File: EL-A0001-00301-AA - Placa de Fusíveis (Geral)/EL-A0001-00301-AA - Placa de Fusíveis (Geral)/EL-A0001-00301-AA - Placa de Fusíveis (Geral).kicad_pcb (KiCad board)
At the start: 2 copper layers, 159 x 109 mm, 25 parts, among them J1 1-776087-1, J10 AUX_POWER, J4 DC_CONVERTER, J5 VBAT, J6 UNFUSED, J7 CS_POWER, J9 ISOL_POWER

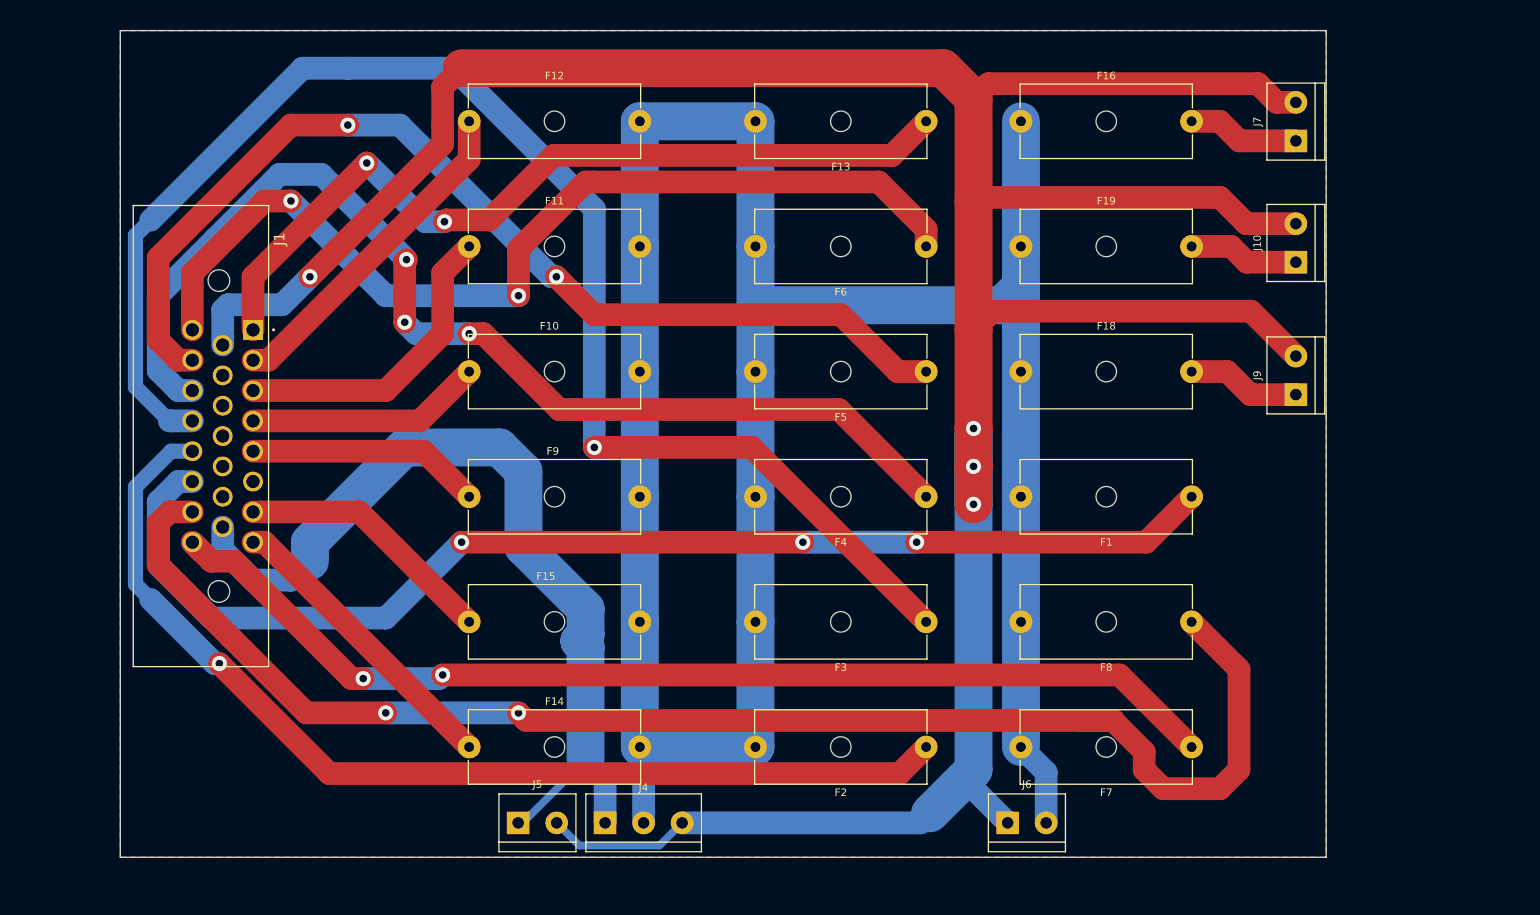
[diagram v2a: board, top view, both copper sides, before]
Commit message: FIX: panel border
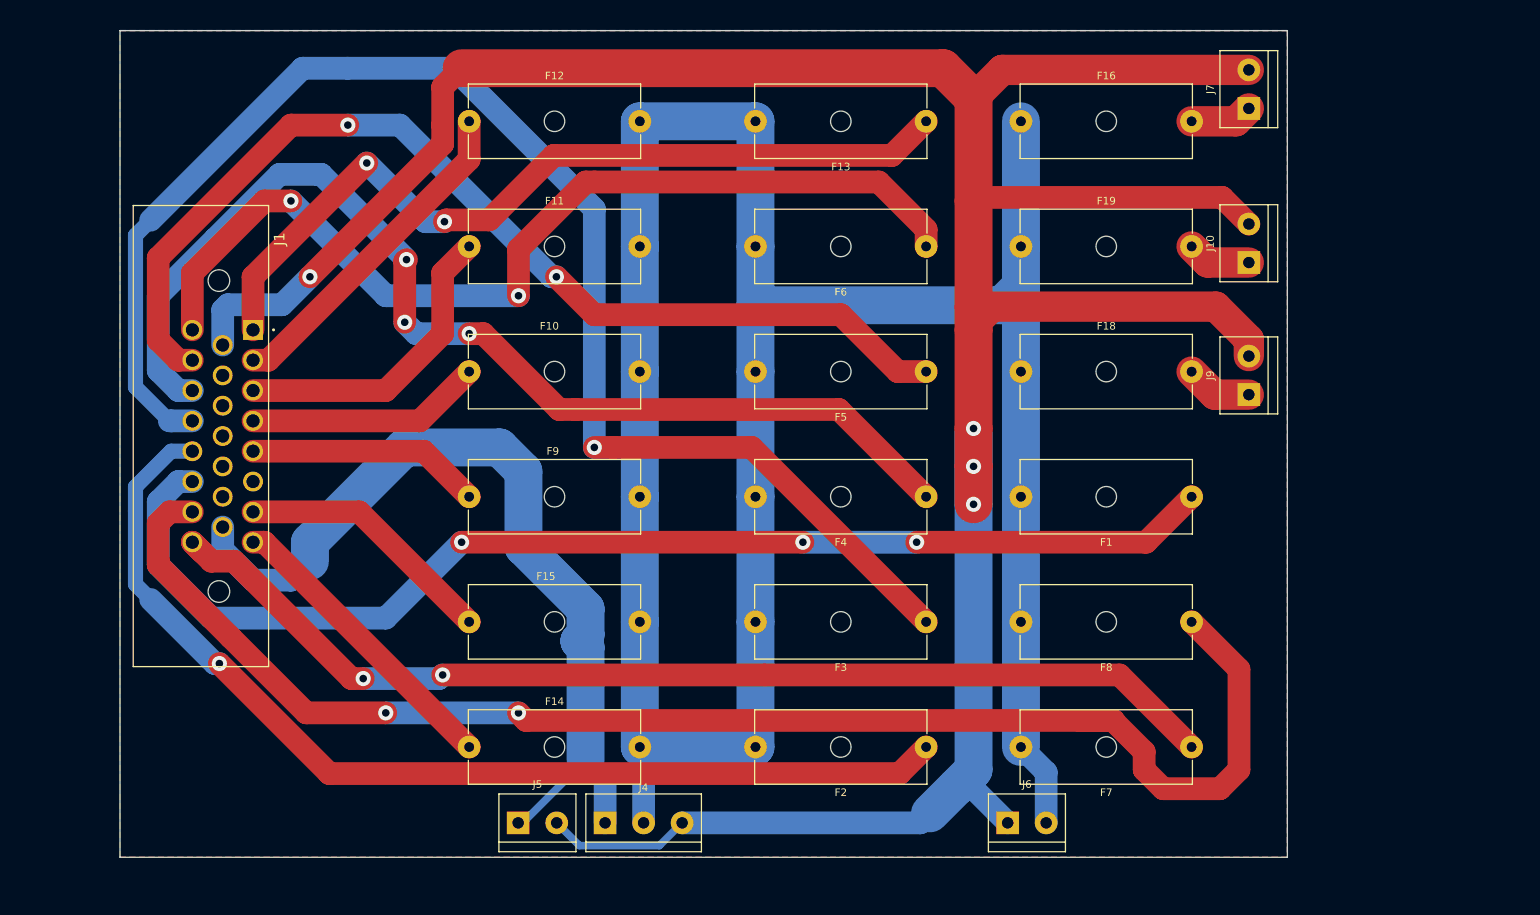
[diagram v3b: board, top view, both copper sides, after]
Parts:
- moved J7 7.53 mm to (177.8, 48.3)
- moved J10 6.20 mm to (177.8, 68.6)
- moved J9 6.20 mm to (177.8, 86.0)
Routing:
- net GNDREF: track 424.9 -> 412.8 mm
- net Net-(J7-Pad1): track 14.8 -> 8.25 mm
- net Net-(F18-Pad2): track 15.0 -> 8.81 mm
- net Net-(F19-Pad2): track 14.6 -> 8.43 mm
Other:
- board size 159 x 109 mm -> 153.9 x 109 mm
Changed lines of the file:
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@@
     (pad "2" thru_hole circle (at 22.5 0) (size 3 3) (drill 1.3) (layers *.Cu *.Mask)
       (net 2 "12V") (pintype "passive"))
-    (model "${KICAD6_3DMODEL_DIR}/Fuse.3dshapes/Fuseholder_Cylinder-5x20mm_Schurter_0031_8201_Horizontal_Open.wrl"
+    (model "${KICAD6_3DMODEL_DIR}/Fuse.3dshapes/Fuseholder_Cylinder-5x20mm_Schurter_0031_8201_Horizontal_Open.step"
       (offset (xyz 0 0 0))
       (scale (xyz 1 1 1))
@@
   )
   (footprint "TerminalBlock:TerminalBlock_bornier-2_P5.08mm" (layer "F.Cu")
-    (at 184 68.54 90)
+    (at 177.8 68.58 90)
     (descr "simple 2-pin terminal block, pitch 5.08mm, revamped version of bornier2")
     (tags "terminal block bornier2")
@@
   )
   (footprint "TerminalBlock:TerminalBlock_bornier-2_P5.08mm" (layer "F.Cu")
-    (at 184 52.54 90)
+    (at 177.8 48.26 90)
     (descr "simple 2-pin terminal block, pitch 5.08mm, revamped version of bornier2")
     (tags "terminal block bornier2")
@@
     (pad "23" thru_hole circle locked (at 28 8 270) (size 2.625 2.625) (drill 1.75) (layers *.Cu *.Mask)
       (net 16 "Net-(J1-Pad23)") (pinfunction "23") (pintype "passive"))
+    (model "C:/Users/Cheetah E-Racing/Documents/tele/Placas/Componentes/Ampseal 23/1-776087-1.step"
+      (offset (xyz 14 -36 12.5))
+      (scale (xyz 1 1 1))
+      (rotate (xyz -90 0 0))
+    )
   )
   (footprint "Fuse:Fuseholder_Cylinder-5x20mm_Schurter_0031_8201_Horizontal_Open" (layer "F.Cu")
@@
     (pad "2" thru_hole circle (at 5.08 0) (size 3 3) (drill 1.52) (layers *.Cu *.Mask)
       (net 2 "12V") (pinfunction "Pin_2") (pintype "passive"))
-    (model "${KICAD6_3DMODEL_DIR}/TerminalBlock.3dshapes/TerminalBlock_bornier-2_P5.08mm.wrl"
-      (offset (xyz 2.539999962 0 0))
+    (model "${KICAD6_3DMODEL_DIR}/TerminalBlock_Phoenix.3dshapes/TerminalBlock_Phoenix_MKDS-3-2-5.08_1x02_P5.08mm_Horizontal.step"
+      (offset (xyz 0 0 0))
       (scale (xyz 1 1 1))
       (rotate (xyz 0 0 0))
@@
   )
   (footprint "TerminalBlock:TerminalBlock_bornier-2_P5.08mm" (layer "F.Cu")
-    (at 184 86 90)
+    (at 177.8 86 90)
     (descr "simple 2-pin terminal block, pitch 5.08mm, revamped version of bornier2")
     (tags "terminal block bornier2")
@@
     (pad "2" thru_hole circle (at 22.5 0) (size 3 3) (drill 1.3) (layers *.Cu *.Mask)
       (net 2 "12V") (pintype "passive"))
-    (model "${KICAD6_3DMODEL_DIR}/Fuse.3dshapes/Fuseholder_Cylinder-5x20mm_Schurter_0031_8201_Horizontal_Open.wrl"
+    (model "${KICAD6_3DMODEL_DIR}/Fuse.3dshapes/Fuseholder_Cylinder-5x20mm_Schurter_0031_8201_Horizontal_Open.step"
       (offset (xyz 0 0 0))
       (scale (xyz 1 1 1))
@@
     )
   )
-  (gr_rect (start 29 38) (end 188 147) (layer "Edge.Cuts") (width 0.1) (fill none))
+  (gr_rect (start 28.96 38) (end 182.88 147) (layer "Edge.Cuts") (width 0.1) (fill none))
   (segment (start 164.25 105.46) (end 134 105.46) (width 3) (layer "F.Cu") (net 1))
   (segment (start 119 105.46) (end 74 105.46) (width 3) (layer "F.Cu") (net 1))
@@
   (segment (start 48 105.46) (end 46.5 105.46) (width 3) (layer "F.Cu") (net 10))
   (segment (start 75 132.46) (end 48 105.46) (width 3) (layer "F.Cu") (net 10))
-  (segment (start 170.25 82.96) (end 174.96 82.96) (width 3) (layer "F.Cu") (net 11))
-  (segment (start 174.96 82.96) (end 178 86) (width 3) (layer "F.Cu") (net 11))
-  (segment (start 178 86) (end 184 86) (width 3) (layer "F.Cu") (net 11))
-  (segment (start 177.54 68.54) (end 175.46 66.46) (width 3) (layer "F.Cu") (net 12))
-  (segment (start 184 68.54) (end 177.54 68.54) (width 3) (layer "F.Cu") (net 12))
-  (segment (start 175.46 66.46) (end 170.25 66.46) (width 3) (layer "F.Cu") (net 12))
+  (segment (start 170.25 82.96) (end 173.29 86) (width 4) (layer "F.Cu") (net 11))
+  (segment (start 173.29 86) (end 177.8 86) (width 4) (layer "F.Cu") (net 11))
+  (segment (start 172.37 68.58) (end 177.8 68.58) (width 4) (layer "F.Cu") (net 12))
+  (segment (start 170.25 66.46) (end 172.37 68.58) (width 4) (layer "F.Cu") (net 12))
   (segment (start 64 85.46) (end 46.5 85.46) (width 3) (layer "F.Cu") (net 13))
   (segment (start 75 66.46) (end 71.5 69.96) (width 3) (layer "F.Cu") (net 13))
@@
   (segment (start 46.5 101.46) (end 60.5 101.46) (width 3) (layer "F.Cu") (net 19))
   (segment (start 60.5 101.46) (end 75 115.96) (width 3) (layer "F.Cu") (net 19))
-  (segment (start 173.96 49.96) (end 176.54 52.54) (width 3) (layer "F.Cu") (net 20))
-  (segment (start 176.54 52.54) (end 184 52.54) (width 3) (layer "F.Cu") (net 20))
-  (segment (start 170.25 49.96) (end 173.96 49.96) (width 3) (layer "F.Cu") (net 20))
+  (segment (start 170.25 49.96) (end 176.1 49.96) (width 4) (layer "F.Cu") (net 20))
+  (segment (start 176.1 49.96) (end 177.8 48.26) (width 4) (layer "F.Cu") (net 20))
   (segment (start 71.5 45.46) (end 74 42.96) (width 3) (layer "F.Cu") (net 21))
   (segment (start 143.46 45) (end 141.5 46.96) (width 3) (layer "F.Cu") (net 21))
+  (segment (start 174.3 60) (end 177.8 63.5) (width 3) (layer "F.Cu") (net 21))
+  (segment (start 177.8 80.92) (end 177.8 78.74) (width 4) (layer "F.Cu") (net 21))
   (segment (start 74 42.96) (end 137.5 42.96) (width 5) (layer "F.Cu") (net 21))
-  (segment (start 179 45) (end 143.46 45) (width 3) (layer "F.Cu") (net 21))
-  (segment (start 177.46 63.46) (end 174 60) (width 3) (layer "F.Cu") (net 21))
+  (segment (start 145.28 43.18) (end 141.5 46.96) (width 4) (layer "F.Cu") (net 21))
   (segment (start 141.5 46.96) (end 141.5 60.5) (width 5) (layer "F.Cu") (net 21))
   (segment (start 144 75) (end 141.5 77.5) (width 3) (layer "F.Cu") (net 21))
   (segment (start 141.5 77.5) (end 141.5 90.46) (width 5) (layer "F.Cu") (net 21))
-  (segment (start 181.46 47.46) (end 179 45) (width 3) (layer "F.Cu") (net 21))
-  (segment (start 141.5 60.5) (end 141.5 77.5) (width 5) (layer "F.Cu") (net 21))
-  (segment (start 184 63.46) (end 177.46 63.46) (width 3) (layer "F.Cu") (net 21))
+  (segment (start 142 60) (end 174.3 60) (width 3) (layer "F.Cu") (net 21))
+  (segment (start 177.8 78.74) (end 173.46 74.4) (width 4) (layer "F.Cu") (net 21))
+  (segment (start 141.5 60.5) (end 141.5 74.4) (width 5) (layer "F.Cu") (net 21))
   (segment (start 141.5 95.46) (end 141.5 100.46) (width 5) (layer "F.Cu") (net 21))
-  (segment (start 184 80.92) (end 178.08 75) (width 3) (layer "F.Cu") (net 21))
   (segment (start 137.5 42.96) (end 141.5 46.96) (width 5) (layer "F.Cu") (net 21))
+  (segment (start 177.8 43.18) (end 145.28 43.18) (width 4) (layer "F.Cu") (net 21))
   (segment (start 71.5 50.46) (end 71.5 45.46) (width 3) (layer "F.Cu") (net 21))
-  (segment (start 142 60) (end 141.5 60.5) (width 3) (layer "F.Cu") (net 21))
   (segment (start 141.5 90.46) (end 141.5 95.46) (width 5) (layer "F.Cu") (net 21))
-  (segment (start 174 60) (end 142 60) (width 3) (layer "F.Cu") (net 21))
-  (segment (start 178.08 75) (end 144 75) (width 3) (layer "F.Cu") (net 21))
+  (segment (start 173.46 74.4) (end 141.5 74.4) (width 4) (layer "F.Cu") (net 21))
   (segment (start 54 70.46) (end 71.5 52.96) (width 3) (layer "F.Cu") (net 21))
+  (segment (start 141.5 74.4) (end 141.5 77.5) (width 5) (layer "F.Cu") (net 21))
   (segment (start 71.5 52.96) (end 71.5 50.46) (width 3) (layer "F.Cu") (net 21))
-  (segment (start 184 47.46) (end 181.46 47.46) (width 3) (layer "F.Cu") (net 21))
+  (segment (start 141.5 60.5) (end 142 60) (width 3) (layer "F.Cu") (net 21))
   (via (at 141.5 90.46) (size 2) (drill 1) (layers "F.Cu" "B.Cu") (net 21))
   (via (at 141.5 95.46) (size 2) (drill 1) (layers "F.Cu" "B.Cu") (net 21))
@@
     (connect_pads (clearance 0.508))
     (min_thickness 0.254) (filled_areas_thickness no)
-    (fill (thermal_gap 0.508) (thermal_bridge_width 0.508))
+    (fill yes (thermal_gap 0.508) (thermal_bridge_width 0.508))
     (polygon
       (pts
-        (xy 188 147)
-        (xy 29 147)
-        (xy 29 38)
-        (xy 188 38)
+        (xy 182.88 147)
+        (xy 28.96 147)
+        (xy 28.96 38)
+        (xy 182.88 38)
       )
     )
@@
     (connect_pads (clearance 0.508))
     (min_thickness 0.254) (filled_areas_thickness no)
-    (fill (thermal_gap 0.508) (thermal_bridge_width 0.508))
+    (fill yes (thermal_gap 0.508) (thermal_bridge_width 0.508))
     (polygon
       (pts
-        (xy 188 147)
-        (xy 29 147)
-        (xy 29 38)
-        (xy 188 38)
+        (xy 182.88 147)
+        (xy 28.96 147)
+        (xy 28.96 38)
+        (xy 182.88 38)
       )
     )

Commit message: MOD: placa de fusiveis nova
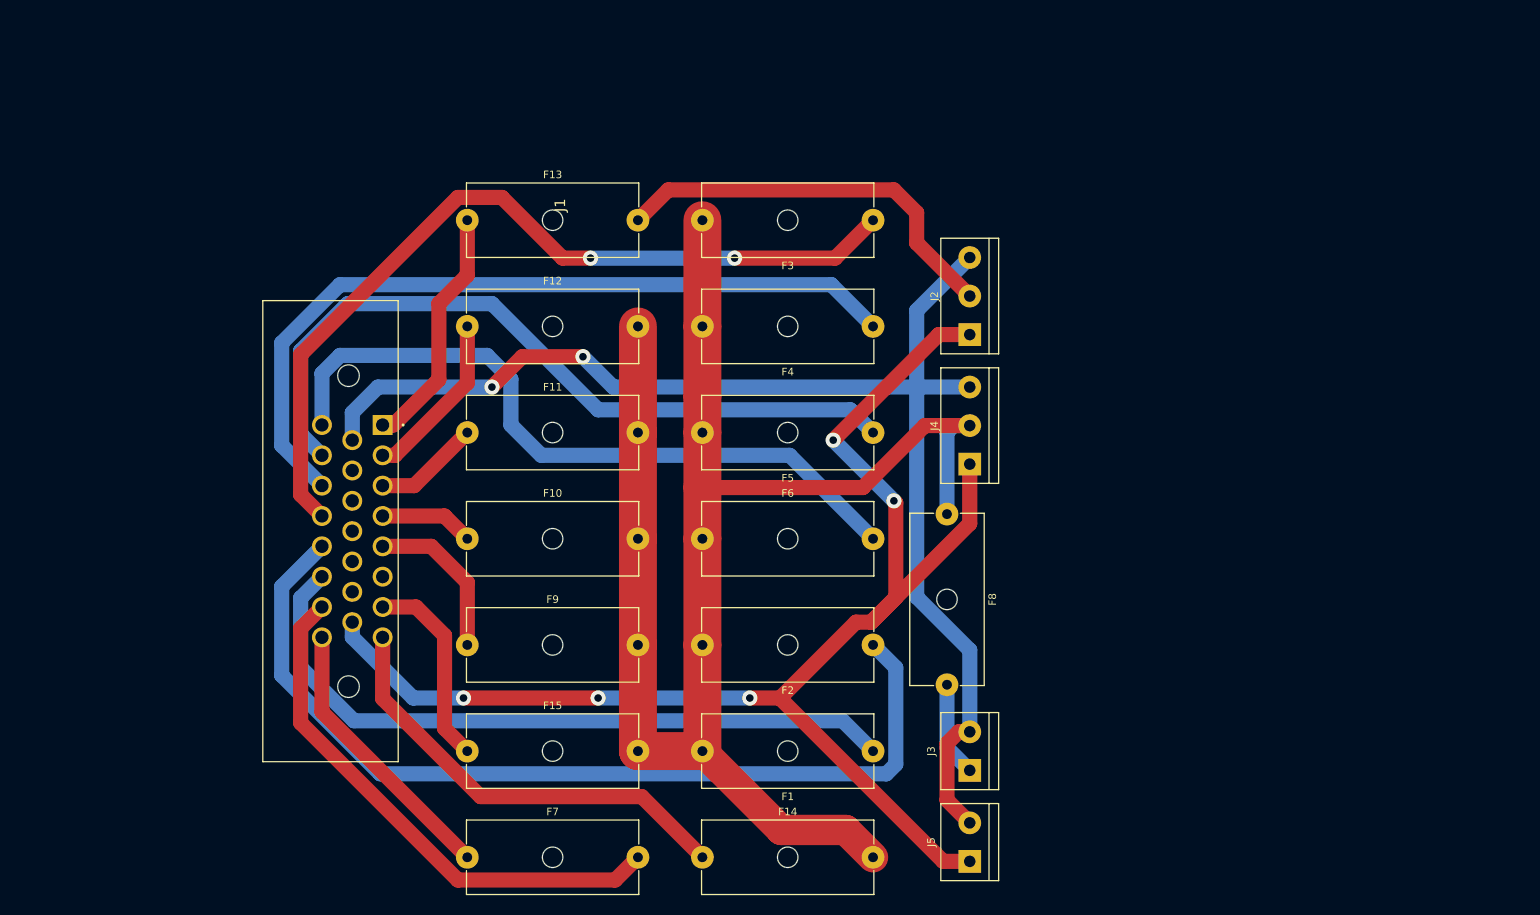
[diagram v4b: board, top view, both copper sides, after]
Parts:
- removed F16, F18, F19: Fuse, Fuse:Fuseholder_Cylinder-5x20mm_Schurter_0031_8201_Horizontal_Open
- removed J10: AUX_POWER, TerminalBlock:TerminalBlock_bornier-2_P5.08mm
- removed J6: UNFUSED, TerminalBlock:TerminalBlock_bornier-2_P5.08mm
- removed J7: CS_POWER, TerminalBlock:TerminalBlock_bornier-2_P5.08mm
- removed J9: ISOL_POWER, TerminalBlock:TerminalBlock_bornier-2_P5.08mm
- added J2: BUCK_SHUT, TerminalBlock:TerminalBlock_bornier-3_P5.08mm, F.Cu at (141.0, 78.1)
- added J3: SPLIT_POWER, TerminalBlock:TerminalBlock_bornier-2_P5.08mm, F.Cu at (141.0, 135.5)
- F13: value Fuse -> SHUT_FUSE
- F7: value Fuse -> GLV_FUSE
- F8: value Fuse -> SPLIT_FUSE
- moved F7 96.6 mm to (74.8, 147.0), turned to 0 degrees
- moved J4 67.4 mm to (141.0, 95.2), turned to 90 degrees
- moved F13 61.9 mm to (74.8, 63.0), turned to 0 degrees
- moved J5 59.8 mm to (141.0, 147.5), turned to 90 degrees
- moved F1 53.7 mm to (128.2, 133.0)
- moved F3 53.4 mm to (128.2, 63.0)
- moved F6 39.2 mm to (128.2, 105.0)
- moved F8 35.2 mm to (138.0, 101.8), turned to -90 degrees
- moved F14 34.0 mm to (105.8, 147.0)
- moved F12 27.0 mm to (74.8, 77.0)
- moved F11 24.5 mm to (74.8, 91.0)
- moved F4 23.5 mm to (128.2, 77.0)
- moved F10 22.0 mm to (74.8, 105.0)
- moved J1 21.2 mm to (63.6, 90.0)
- moved F9 19.5 mm to (74.8, 119.0)
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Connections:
- net GNDREF renamed GND
- net Net-(J1-Pad15) renamed VBAT
- F13 pad 2: 12V -> Net-(J2-Pad2)
- F7 pad 2: 12V -> Net-(J1-Pad22)
- F8 pad 1: Net-(J1-Pad22) -> 12V
- F8 pad 2: 12V -> Net-(F8-Pad2)
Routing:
- net GND: track 412.8 -> 173.4 mm, vias 4 -> 2
- net Net-(J1-Pad22): track 194.4 -> 70.7 mm, vias 2 -> 0
- net 12V: track 335.6 -> 215.6 mm
- net Net-(F7-Pad1): track 145.2 -> 36.9 mm, vias 2 -> 0
- net Net-(F3-Pad1): track 191.4 -> 111.9 mm, vias 1 -> 2
- net Net-(J1-Pad1): track 110.7 -> 32.5 mm, vias 2 -> 0
- net VBAT: track 118.1 -> 190.6 mm, vias 0 -> 5
- net Net-(F1-Pad1): track 159.7 -> 93.2 mm, vias 3 -> 0
- net Net-(J2-Pad2): track 0.00 -> 53.5 mm
- net Net-(F4-Pad1): track 145.8 -> 104.4 mm, vias 3 -> 0
- net Net-(F5-Pad1): track 138.4 -> 100.0 mm, vias 2 -> 0
- net Net-(F6-Pad1): track 128.0 -> 94.0 mm, vias 2 -> 0
- net Net-(F11-Pad1): track 41.1 -> 14.1 mm
- net Net-(F12-Pad1): track 44.5 -> 22.6 mm
- net Net-(F14-Pad1): track 39.7 -> 58.9 mm
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- removed copper zone on B.Cu, net 12V
- removed copper zone on F.Cu, net GND
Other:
- board outline removed
